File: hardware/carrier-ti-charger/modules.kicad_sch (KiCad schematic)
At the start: 21 parts, among them J10 J_ADS_MAIN ADSBee J5, J11 J_ADS_GNSS ADSBee J4, J5 J_GNSS GPS-18037 J5, J6 J_ESP_A support, J7 J_ESP_B power/UART, J8 J_ESP_C I2C, J9 J_ESP_D support, U11 LM73100RPWR, U12 LM73100RPWR

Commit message: TI charger
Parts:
- added C51, C52: 22u 10V X7R, Capacitor_SMD:C_0805_2012Metric, symbol Device:C
- C38, C39: value 100n -> 100n 50V
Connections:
- net ESP_5V: now also C51.1, C52.1
- net GND: now also C51.2, C52.2
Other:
- moved on the sheet: C25

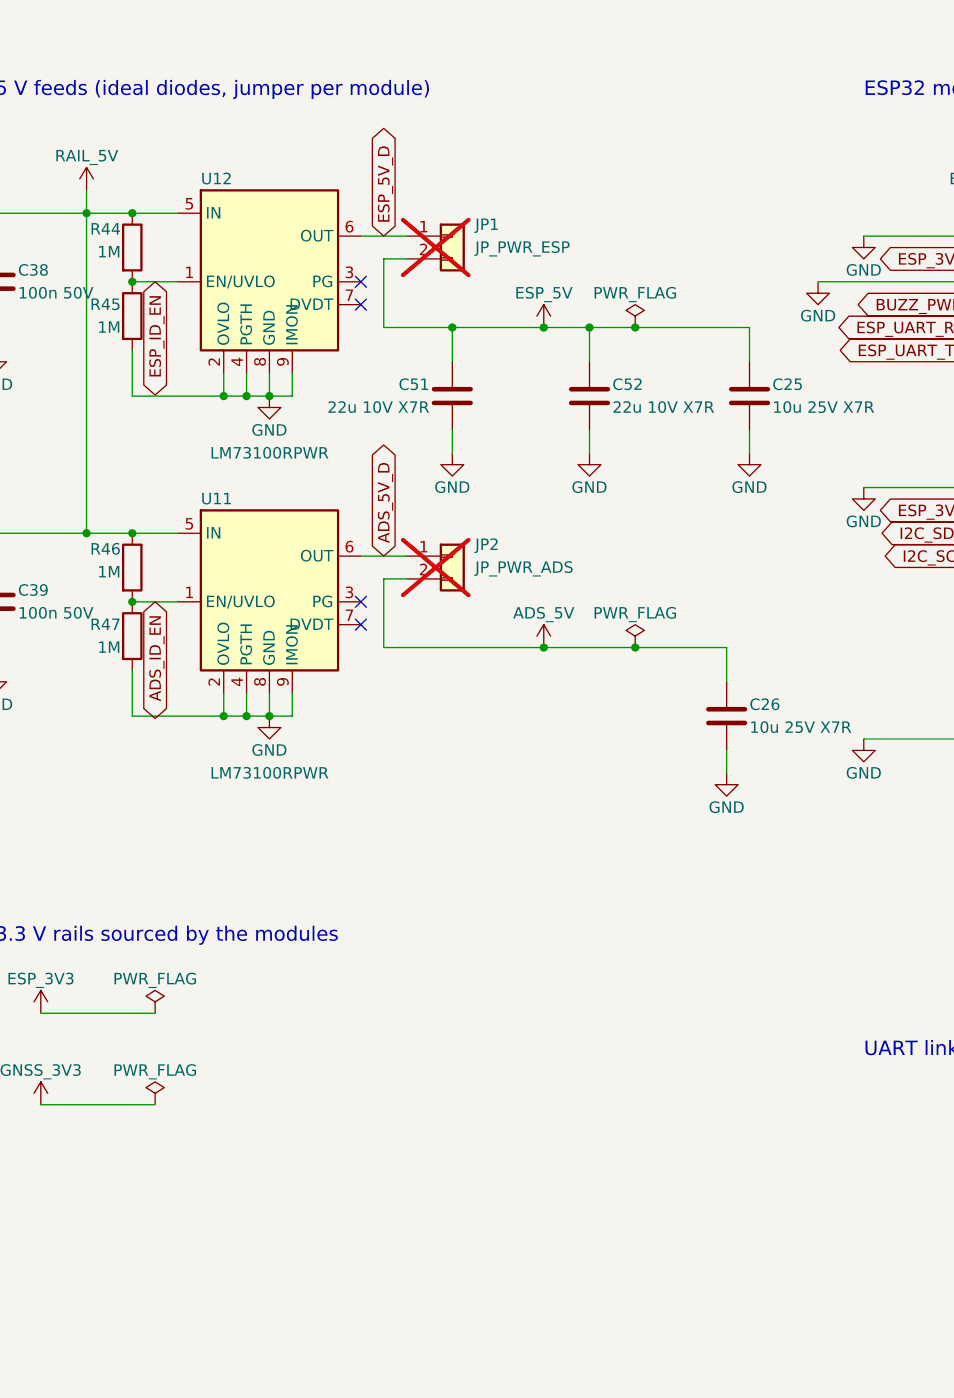
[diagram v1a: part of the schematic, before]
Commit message: Switch parts (BMP580, TPS259474L) due to stock shortage.
Also, add overvoltage (OVLO) protection.
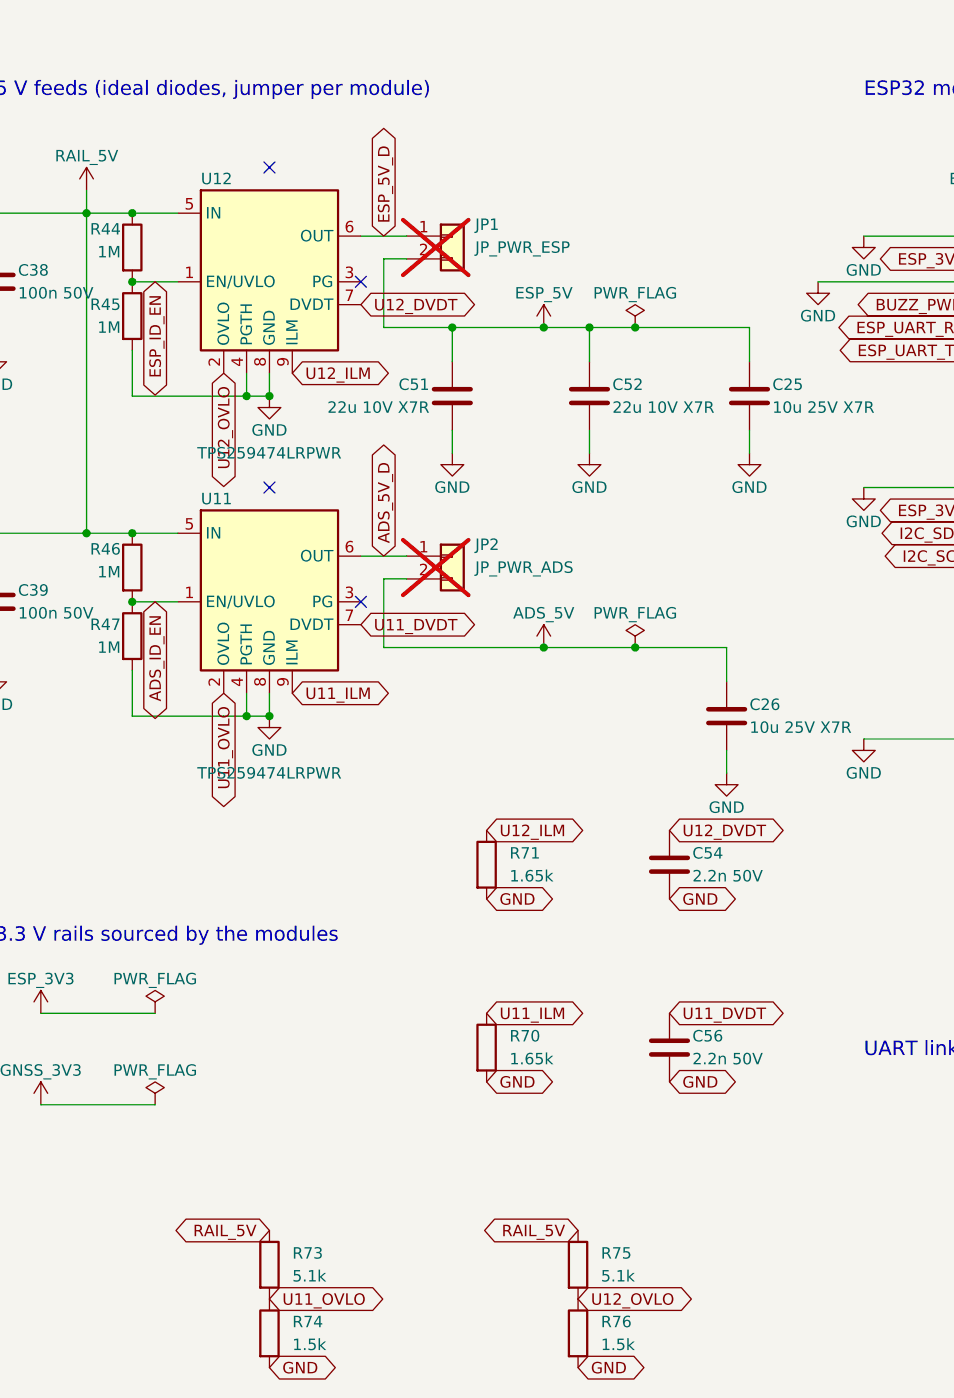
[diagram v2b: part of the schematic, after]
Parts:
- added C54, C56: 2.2n 50V, Capacitor_SMD:C_0603_1608Metric, symbol Device:C
- added R70, R71: 1.65k, Resistor_SMD:R_0603_1608Metric, symbol Device:R
- added R73, R75: 5.1k, carrier:R_0402_1005Metric_NoSilk, symbol Device:R
- added R74, R76: 1.5k, carrier:R_0402_1005Metric_NoSilk, symbol Device:R
- U11, U12: value LM73100RPWR -> TPS259474LRPWR; symbol carrier:LM73100RPW -> carrier:TPS259474LRPW; LCSC C3210761 -> C2864845
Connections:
- net GND: now also C54.2, C56.2, R70.2, R71.2, R74.2, R76.2; no longer U11.2 (OVLO), U11.9 (IMON), U12.2 (OVLO), U12.9 (IMON)
- net RAIL_5V: now also R73.1, R75.1
- net U12_DVDT: now reaches U12.7 (DVDT)
- net U12_DVDT: now also C54.1
- net U11_DVDT: now reaches U11.7 (DVDT)
- net U11_DVDT: now also C56.1
- new net U11_ILM: R70.1, U11.9 (ILM)
- new net U11_OVLO: R73.2, R74.1, U11.2 (OVLO)
- new net U12_ILM: R71.1, U12.9 (ILM)
- new net U12_OVLO: R75.2, R76.1, U12.2 (OVLO)

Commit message: Other MH's.
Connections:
- net ADS_5V renamed +ADS_5V
- net ADS_5V_D renamed +ADS_5V_D
- net ESP_3V3 renamed +ESP_3V3
- net ESP_5V renamed +ESP_5V
- net ESP_5V_D renamed +ESP_5V_D
- net GNSS_3V3 renamed +GNSS_3V3
- net RAIL_5V renamed +5V

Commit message: Rule alignment.
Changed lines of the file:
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@@
+		)
+	)
+	(symbol
+		(lib_id "power:PWR_FLAG")
+		(at 91.44 55.88 0)
+		(unit 1)
+		(body_style 1)
+		(exclude_from_sim no)
+		(in_bom yes)
+		(on_board yes)
+		(in_pos_files yes)
+		(dnp no)
+		(property "Reference" "#FLG012"
+			(at 91.44 53.34 0)
+			(hide yes)
+			(show_name no)
+			(do_not_autoplace no)
+			(effects
+				(font
+					(size 1.27 1.27)
+				)
+			)
+		)
+		(property "Value" "PWR_FLAG"
+			(at 91.44 52.07 0)
+			(show_name no)
+			(do_not_autoplace no)
+			(effects
+				(font
+					(size 1.27 1.27)
+				)
+			)
+		)
+		(property "Footprint" ""
+			(at 91.44 55.88 0)
+			(hide yes)
+			(show_name no)
+			(do_not_autoplace no)
+			(effects
+				(font
+					(size 1.27 1.27)
+				)
+			)
+		)
+		(property "Datasheet" ""
+			(at 91.44 55.88 0)
+			(hide yes)
+			(show_name no)
+			(do_not_autoplace no)
+			(effects
+				(font
+					(size 1.27 1.27)
+				)
+			)
+		)
+		(property "Description" "Power symbol creates a global label with name \"PWR_FLAG\""
+			(at 91.44 55.88 0)
+			(hide yes)
+			(show_name no)
+			(do_not_autoplace no)
+			(effects
+				(font
+					(size 1.27 1.27)
+				)
+			)
+		)
+		(pin "1"
+		)
+		(instances
+			(project "carrier"
+				(path "/1d76d2ec-7795-4c71-8167-b1182c3ebc1d/3f53ac70-9f38-49d5-b028-e652ebac7ccc"
+					(reference "#FLG012")
+					(unit 1)
+				)
+			)
+		)
+	)
+	(global_label "+ESP_5V_D"
+		(shape bidirectional)
+		(at 91.44 55.88 0)
+		(fields_autoplaced yes)
+		(effects
+				(font
+					(size 1.27 1.27)
+				)
+				(justify left)
+			)
+		(property "Intersheetrefs" "${INTERSHEET_REFS}"
+			(at 91.44 55.88 0)
+			(hide yes)
+			(show_name no)
+			(do_not_autoplace no)
+			(effects
+				(font
+					(size 1.27 1.27)
+				)
+				(justify left)
+			)
+		)
+	)
+	(symbol
+		(lib_id "power:PWR_FLAG")
+		(at 91.44 96.52 0)
+		(unit 1)
+		(body_style 1)
+		(exclude_from_sim no)
+		(in_bom yes)
+		(on_board yes)
+		(in_pos_files yes)
+		(dnp no)
+		(property "Reference" "#FLG013"
+			(at 91.44 93.98 0)
+			(hide yes)
+			(show_name no)
+			(do_not_autoplace no)
+			(effects
+				(font
+					(size 1.27 1.27)
+				)
+			)
+		)
+		(property "Value" "PWR_FLAG"
+			(at 91.44 92.71 0)
+			(show_name no)
+			(do_not_autoplace no)
+			(effects
+				(font
+					(size 1.27 1.27)
+				)
+			)
+		)
+		(property "Footprint" ""
+			(at 91.44 96.52 0)
+			(hide yes)
+			(show_name no)
+			(do_not_autoplace no)
+			(effects
+				(font
+					(size 1.27 1.27)
+				)
+			)
+		)
+		(property "Datasheet" ""
+			(at 91.44 96.52 0)
+			(hide yes)
+			(show_name no)
+			(do_not_autoplace no)
+			(effects
+				(font
+					(size 1.27 1.27)
+				)
+			)
+		)
+		(property "Description" "Power symbol creates a global label with name \"PWR_FLAG\""
+			(at 91.44 96.52 0)
+			(hide yes)
+			(show_name no)
+			(do_not_autoplace no)
+			(effects
+				(font
+					(size 1.27 1.27)
+				)
+			)
+		)
+		(pin "1"
+		)
+		(instances
+			(project "carrier"
+				(path "/1d76d2ec-7795-4c71-8167-b1182c3ebc1d/3f53ac70-9f38-49d5-b028-e652ebac7ccc"
+					(reference "#FLG013")
+					(unit 1)
+				)
+			)
+		)
+	)
+	(global_label "+ADS_5V_D"
+		(shape bidirectional)
+		(at 91.44 96.52 0)
+		(fields_autoplaced yes)
+		(effects
+				(font
+					(size 1.27 1.27)
+				)
+				(justify left)
+			)
+		(property "Intersheetrefs" "${INTERSHEET_REFS}"
+			(at 91.44 96.52 0)
+			(hide yes)
+			(show_name no)
+			(do_not_autoplace no)
+			(effects
+				(font
+					(size 1.27 1.27)
+				)
+				(justify left)
+			)
 		)
 	)

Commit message: Update resistors for stock availability.
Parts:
- R73, R75: value 5.1k -> 5.36k; footprint carrier:R_0402_1005Metric_NoSilk -> carrier:R_0805_2012Metric_NoSilk; LCSC C25905 -> C706247; MPN 0402WGF5101TCE -> RT0805BRD075K36L; Manufacturer (none) -> YAGEO; TCR 100 ppm/C -> 25 ppm/C; Tolerance 1% -> 0.1%
- R74, R76: LCSC C25867 -> C281775; MPN 0402WGF1501TCE -> RT0402BRD071K5L; Manufacturer (none) -> YAGEO; TCR 100 ppm/C -> 25 ppm/C; Tolerance 1% -> 0.1%
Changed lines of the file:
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@@
 			)
 		)
-		(property "Datasheet" "https://www.lcsc.com/datasheet/C25867.pdf"
+		(property "Datasheet" "https://datasheet.lcsc.com/datasheet/pdf/46d7760c582640714d605308a25a220a.pdf?productCode=C281775"
 			(at 55.88 182.88 0)
 			(hide yes)
@@
 			)
 		)
-		(property "Description" "OVLO divider, 1%, 100 ppm/C, 62.5 mW, 50 V"
+		(property "Description" "OVLO divider, 0.1%, 25 ppm/C, 62.5 mW, 50 V"
 			(at 55.88 182.88 0)
 			(hide yes)
@@
 			)
 		)
-		(property "LCSC" "C25867"
+		(property "LCSC" "C281775"
 			(at 55.88 182.88 0)
 			(hide yes)
@@
 			)
 		)
-		(property "MPN" "0402WGF1501TCE"
+		(property "MPN" "RT0402BRD071K5L"
 			(at 55.88 182.88 0)
 			(hide yes)
@@
 			)
 		)
-		(property "Tolerance" "1%"
+		(property "Tolerance" "0.1%"
 			(at 55.88 182.88 0)
 			(hide yes)
@@
 			)
 		)
-		(property "TCR" "100 ppm/C"
+		(property "TCR" "25 ppm/C"
+			(at 55.88 182.88 0)
+			(hide yes)
+			(show_name no)
+			(do_not_autoplace no)
+			(effects
+				(font
+					(size 1.27 1.27)
+				)
+			)
+		)
+		(property "Manufacturer" "YAGEO"
 			(at 55.88 182.88 0)
 			(hide yes)
@@
 			)
 		)
-		(property "Value" "5.1k"
+		(property "Value" "5.36k"
 			(at 92.71 176.53 0)
 			(show_name no)
@@
 			)
 		)
-		(property "Footprint" "carrier:R_0402_1005Metric_NoSilk"
+		(property "Footprint" "carrier:R_0805_2012Metric_NoSilk"
+			(at 90.17 175.26 0)
+			(hide yes)
+			(show_name no)
+			(do_not_autoplace no)
+			(effects
+				(font
+					(size 1.27 1.27)
+				)
+			)
+		)
+		(property "Datasheet" "https://datasheet.lcsc.com/datasheet/pdf/46d7760c582640714d605308a25a220a.pdf?productCode=C706247"
 			(at 90.17 175.26 0)
 			(hide yes)
@@
 			)
 		)
-		(property "Datasheet" "https://www.lcsc.com/datasheet/C25905.pdf"
+		(property "Description" "OVLO divider, 0.1%, 25 ppm/C, 125 mW, 150 V"
 			(at 90.17 175.26 0)
 			(hide yes)
@@
 			)
 		)
-		(property "Description" "OVLO divider, 1%, 100 ppm/C, 62.5 mW, 50 V"
+		(property "LCSC" "C706247"
 			(at 90.17 175.26 0)
 			(hide yes)
@@
 			)
 		)
-		(property "LCSC" "C25905"
+		(property "MPN" "RT0805BRD075K36L"
 			(at 90.17 175.26 0)
 			(hide yes)
@@
 			)
 		)
-		(property "MPN" "0402WGF5101TCE"
+		(property "Tolerance" "0.1%"
 			(at 90.17 175.26 0)
 			(hide yes)
@@
 			)
 		)
-		(property "Tolerance" "1%"
+		(property "TCR" "25 ppm/C"
 			(at 90.17 175.26 0)
 			(hide yes)
@@
 			)
 		)
-		(property "TCR" "100 ppm/C"
+		(property "Manufacturer" "YAGEO"
 			(at 90.17 175.26 0)
 			(hide yes)
@@
 			)
 		)
-		(property "Datasheet" "https://www.lcsc.com/datasheet/C25867.pdf"
+		(property "Datasheet" "https://datasheet.lcsc.com/datasheet/pdf/46d7760c582640714d605308a25a220a.pdf?productCode=C281775"
 			(at 90.17 182.88 0)
 			(hide yes)
@@
 			)
 		)
-		(property "Description" "OVLO divider, 1%, 100 ppm/C, 62.5 mW, 50 V"
+		(property "Description" "OVLO divider, 0.1%, 25 ppm/C, 62.5 mW, 50 V"
 			(at 90.17 182.88 0)
 			(hide yes)
@@
 			)
 		)
-		(property "LCSC" "C25867"
+		(property "LCSC" "C281775"
 			(at 90.17 182.88 0)
 			(hide yes)
@@
 			)
 		)
-		(property "MPN" "0402WGF1501TCE"
+		(property "MPN" "RT0402BRD071K5L"
 			(at 90.17 182.88 0)
 			(hide yes)
@@
 			)
 		)
-		(property "Tolerance" "1%"
+		(property "Tolerance" "0.1%"
 			(at 90.17 182.88 0)
 			(hide yes)
@@
 			)
 		)
-		(property "TCR" "100 ppm/C"
+		(property "TCR" "25 ppm/C"
+			(at 90.17 182.88 0)
+			(hide yes)
+			(show_name no)
+			(do_not_autoplace no)
+			(effects
+				(font
+					(size 1.27 1.27)
+				)
+			)
+		)
+		(property "Manufacturer" "YAGEO"
 			(at 90.17 182.88 0)
 			(hide yes)
@@
 			)
 		)
-		(property "Value" "5.1k"
+		(property "Value" "5.36k"
 			(at 58.42 176.53 0)
 			(show_name no)
@@
 			)
 		)
-		(property "Footprint" "carrier:R_0402_1005Metric_NoSilk"
+		(property "Footprint" "carrier:R_0805_2012Metric_NoSilk"
+			(at 55.88 175.26 0)
+			(hide yes)
+			(show_name no)
+			(do_not_autoplace no)
+			(effects
+				(font
+					(size 1.27 1.27)
+				)
+			)
+		)
+		(property "Datasheet" "https://datasheet.lcsc.com/datasheet/pdf/46d7760c582640714d605308a25a220a.pdf?productCode=C706247"
 			(at 55.88 175.26 0)
 			(hide yes)
@@
 			)
 		)
-		(property "Datasheet" "https://www.lcsc.com/datasheet/C25905.pdf"
+		(property "Description" "OVLO divider, 0.1%, 25 ppm/C, 125 mW, 150 V"
 			(at 55.88 175.26 0)
 			(hide yes)
@@
 			)
 		)
-		(property "Description" "OVLO divider, 1%, 100 ppm/C, 62.5 mW, 50 V"
+		(property "LCSC" "C706247"
 			(at 55.88 175.26 0)
 			(hide yes)
@@
 			)
 		)
-		(property "LCSC" "C25905"
+		(property "MPN" "RT0805BRD075K36L"
 			(at 55.88 175.26 0)
 			(hide yes)
@@
 			)
 		)
-		(property "MPN" "0402WGF5101TCE"
+		(property "Tolerance" "0.1%"
 			(at 55.88 175.26 0)
 			(hide yes)
@@
 			)
 		)
-		(property "Tolerance" "1%"
+		(property "TCR" "25 ppm/C"
 			(at 55.88 175.26 0)
 			(hide yes)
@@
 			)
 		)
-		(property "TCR" "100 ppm/C"
+		(property "Manufacturer" "YAGEO"
 			(at 55.88 175.26 0)
 			(hide yes)

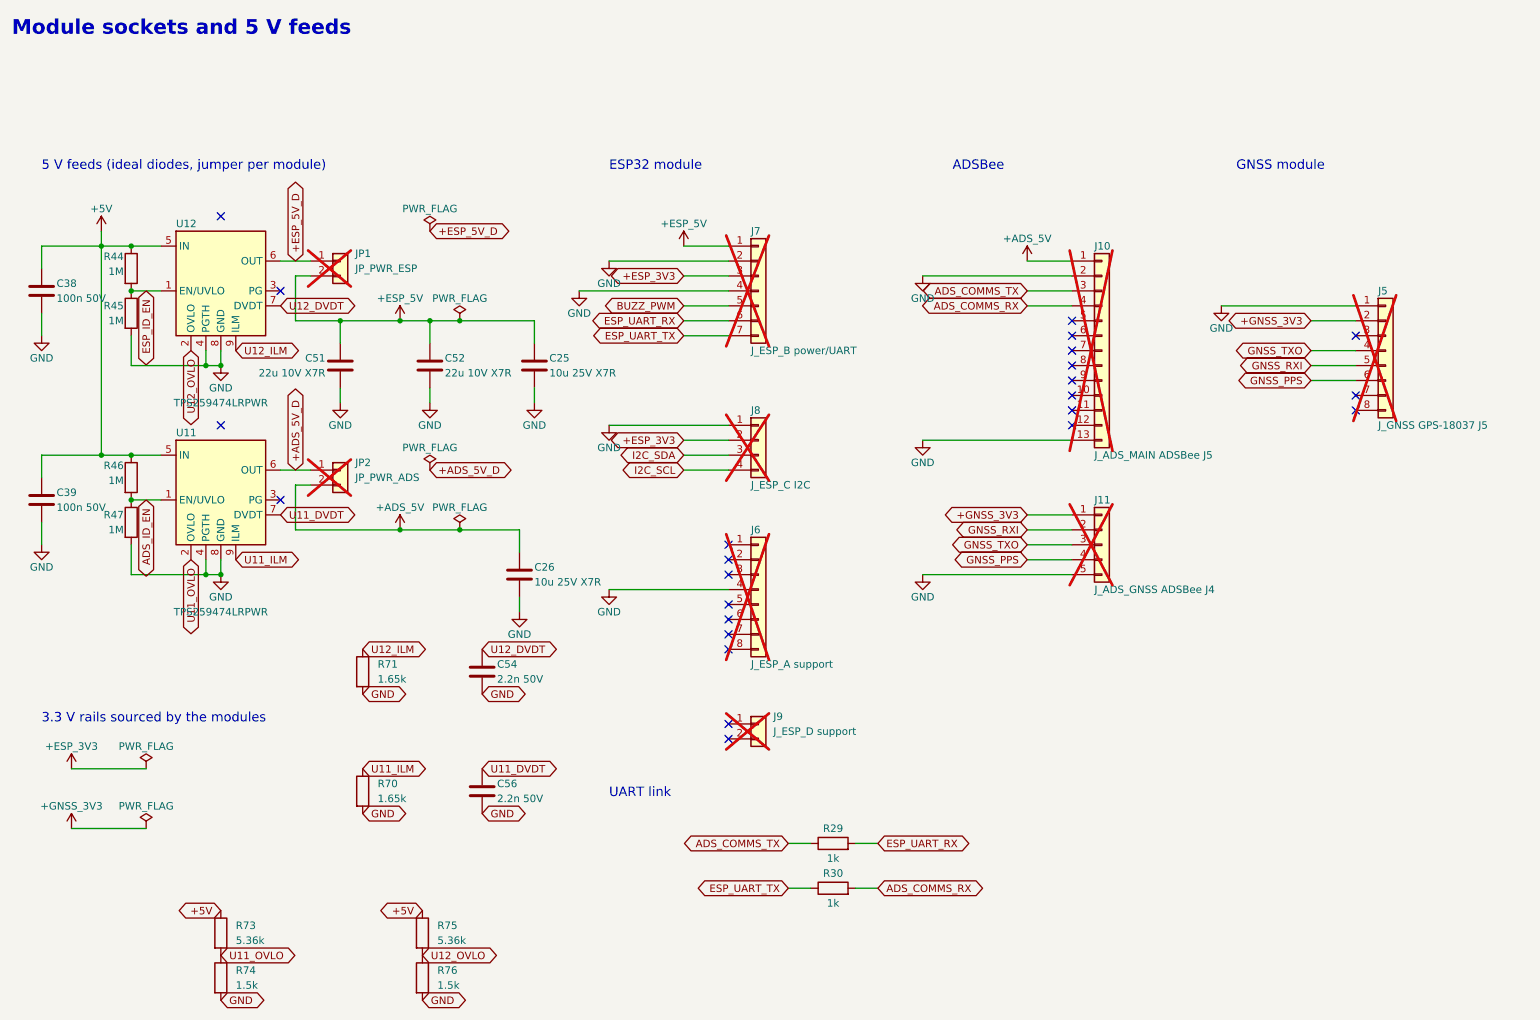
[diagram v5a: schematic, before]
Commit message: Add USB current detection.
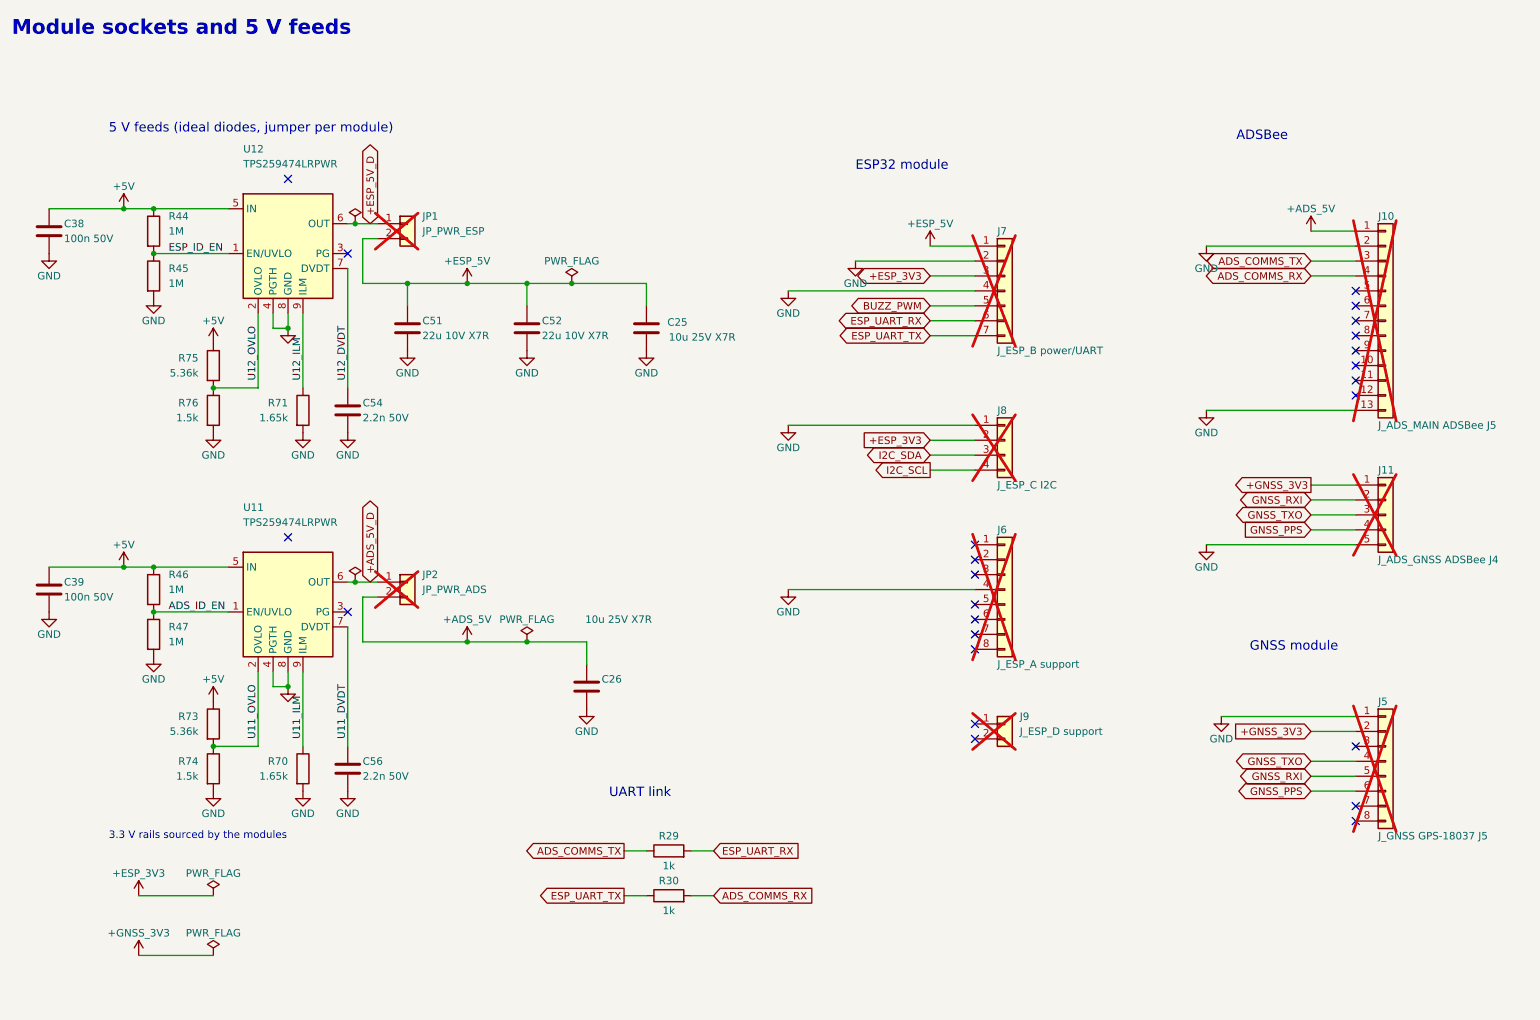
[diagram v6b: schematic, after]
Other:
- moved on the sheet: C25, C26, C38, C39, C51, C52, C54, C56, J10, J11, J5, J6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
